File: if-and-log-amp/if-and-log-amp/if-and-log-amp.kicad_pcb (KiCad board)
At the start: 2 copper layers, 91.7 x 48.8 mm, 74 parts, among them J301 Coax, J305 Conn_01x03, J306 Conn_01x02, J307 Conn_Coaxial, Q301 2N3904, T301 FT37-43 8:2 t, U301 AD603AQ, U302 L78L05_TO92, U303 LM317L_TO92, U304 AD8307AN, U305 CA3140

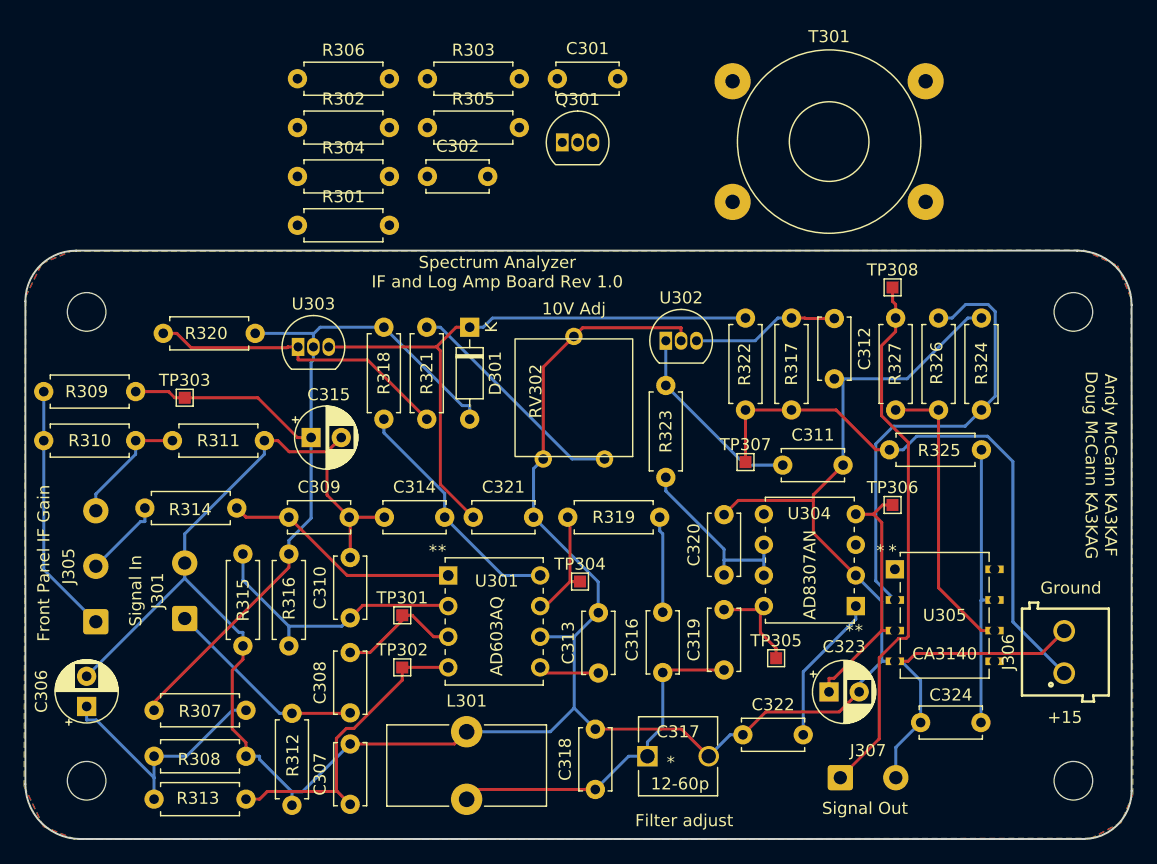
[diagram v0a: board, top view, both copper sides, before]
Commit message: improved if and log amp and second lo/mixer
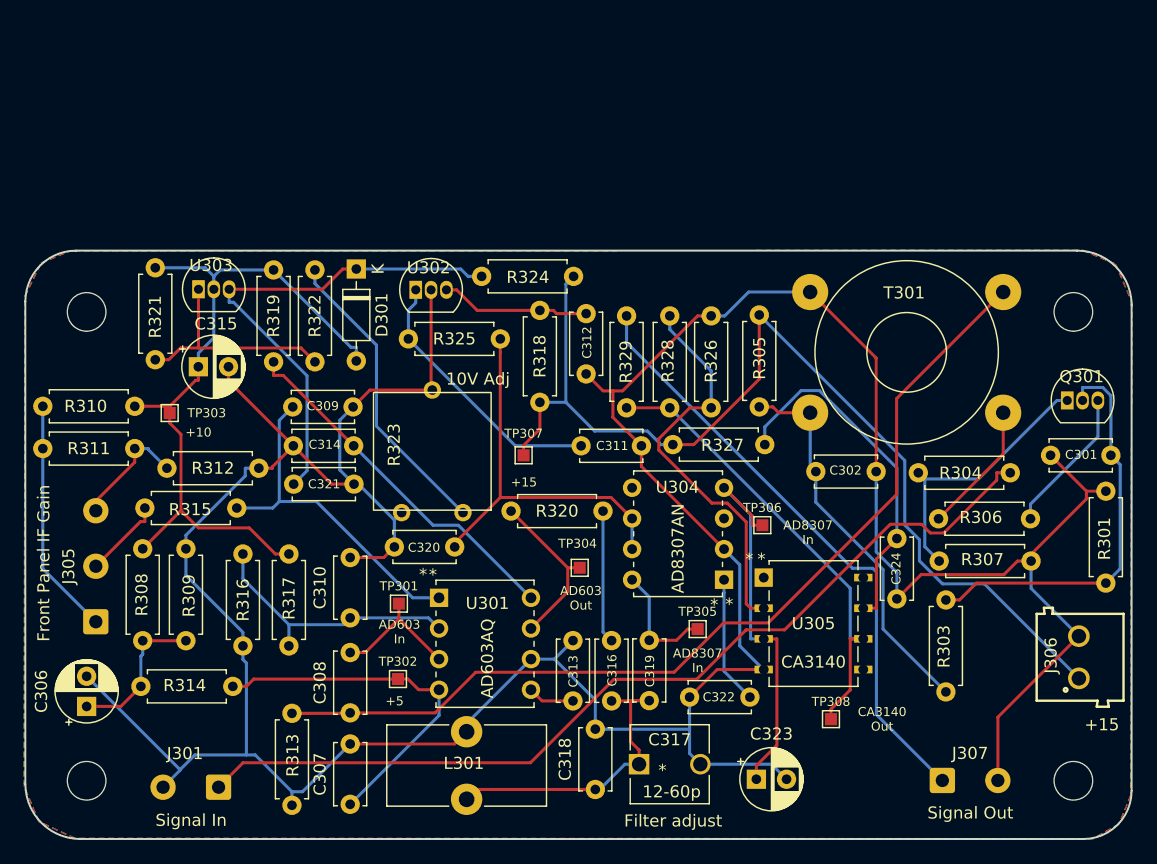
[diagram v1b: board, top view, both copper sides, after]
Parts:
- moved R301 76.9 mm to (184.9, 108.0), turned to 90 degrees
- moved R307 66.5 mm to (171.1, 106.1)
- moved R303 66.2 mm to (171.7, 117.0), turned to 90 degrees
- moved R306 53.4 mm to (171.0, 102.6)
- moved R304 52.2 mm to (169.4, 98.8)
- moved C301 51.4 mm to (180.3, 97.4)
- moved Q301 47.0 mm to (181.7, 92.8)
- moved C302 40.4 mm to (160.9, 98.7)
- moved R305 40.0 mm to (156.2, 85.8), turned to -90 degrees
- moved TP308 36.2 mm to (162.1, 119.3)
- moved C320 22.4 mm to (130.9, 105.0), turned to 180 degrees
- moved R326 22.4 mm to (152.2, 93.4)
- moved R329 22.3 mm to (145.2, 93.4)
- moved R328 22.3 mm to (148.8, 93.4)
- moved R325 21.7 mm to (127.1, 87.7), turned to 0 degrees
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- renumbered R302 to R301, R301 to R303, R303 to R304, R304 to R305, R305 to R306, R306 to R307, R307 to R308, R308 to R309, R309 to R310, R310 to R311, R311 to R312, R312 to R313, R313 to R314, R314 to R315, R315 to R316, R316 to R317, R317 to R318, R318 to R319, R319 to R320, R320 to R321, R321 to R322, RV302 to R323, R322 to R324, R323 to R325, R324 to R326, R325 to R327, R326 to R328, R327 to R329
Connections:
- R328 pad 1: Net-(R326-Pad1) (its old number) -> Net-(R328-Pad1)
- R329 pad 1: Net-(R326-Pad1) (its old number) -> Net-(R328-Pad1)
- TP308 pad 1: Net-(C325-Pad1) -> Net-(R328-Pad1)
- U305 pad 6: Net-(R326-Pad1) (its old number) -> Net-(R328-Pad1)
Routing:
- net /In: track 0.00 -> 77.4 mm
- net Net-(C308-Pad1): track 17.0 -> 78.1 mm
- net GND: track 251.6 -> 300.1 mm
- net Net-(R328-Pad1): track 0.00 -> 38.4 mm
- net /+15: track 48.5 -> 86.1 mm
- net Net-(C301-Pad2): track 0.00 -> 33.9 mm
- net Net-(C302-Pad1): track 0.00 -> 32.2 mm
- net Net-(R326-Pad1) (its old number): track 24.4 -> 0.00 mm
- net Net-(Q301-Pad1): track 0.00 -> 22.5 mm
- net Net-(C320-Pad1): track 15.9 -> 33.0 mm
- net /+10: track 74.6 -> 60.2 mm
- net Net-(Q301-Pad3): track 0.00 -> 12.1 mm
- net Net-(C323-Pad1): track 21.5 -> 32.8 mm
- net Net-(R306-Pad1): track 0.00 -> 11.0 mm
- net Net-(C314-Pad2): track 20.1 -> 30.1 mm
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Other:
- board text added: "+10"
- board text added: "+5"
- board text added: "AD603 In"
- board text added: "AD603 Out"
- board text added: "AD8307 In"
- board text added: "CA3140 Out"
- board text removed: "Ground"

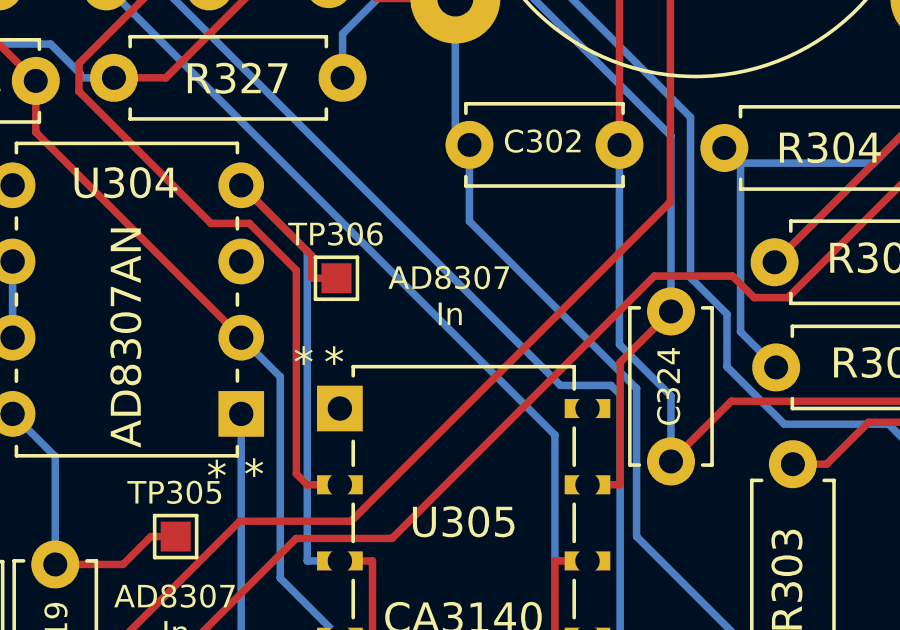
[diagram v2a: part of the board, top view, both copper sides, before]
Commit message: if and log amp - add version 0 pcb to directory
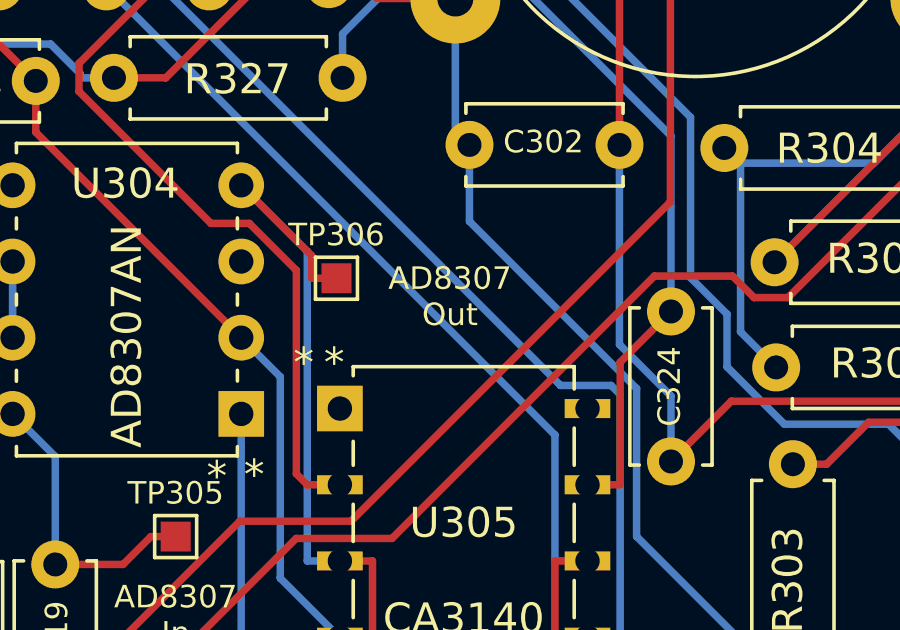
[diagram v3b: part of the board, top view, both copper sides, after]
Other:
- board text added: "AD8307 Out"
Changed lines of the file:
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@@
     (effects (font (size 0.75 0.75) (thickness 0.15)))
   )
-  (gr_text "AD8307\nIn" (at 160.2232 103.7844) (layer "F.SilkS")
+  (gr_text "AD8307\nOut" (at 160.2232 103.7844) (layer "F.SilkS")
     (effects (font (size 0.75 0.75) (thickness 0.15)))
   )

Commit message: IF Log Amp V2
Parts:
- removed C315: 22u, Capacitor_THT:CP_Radial_D5.0mm_P2.50mm
- removed C323: .001u, Capacitor_THT:CP_Radial_D5.0mm_P2.50mm
- removed C324: .1u, Capacitor_THT:C_Disc_D5.0mm_W2.5mm_P5.00mm
- removed J305: Conn_01x03, Connector_Wire:SolderWire-0.5sqmm_1x03_P4.6mm_D0.9mm_OD2.1mm
- removed J306: Conn_01x02, if-log-amp:691103110002
- removed J307: Conn_Coaxial, Connector_Wire:SolderWire-0.5sqmm_1x02_P4.6mm_D0.9mm_OD2.1mm
- removed R329: 1k, Resistor_THT:R_Axial_DIN0207_L6.3mm_D2.5mm_P7.62mm_Horizontal
- added C303: .1u, Capacitor_THT:C_Disc_D5.0mm_W2.5mm_P5.00mm, F.Cu at (101.1, 90.4)
- added C304: .01u, Capacitor_THT:C_Disc_D5.0mm_W2.5mm_P5.00mm, F.Cu at (123.8, 100.4)
- added C305: 100u, Capacitor_THT:CP_Radial_D5.0mm_P2.50mm, F.Cu at (148.4, 119.8)
- added J302: Conn_Coaxial, Connector_Wire:SolderWire-0.5sqmm_1x02_P4.6mm_D0.9mm_OD2.1mm, F.Cu at (166.6, 126.0)
- added J303: +15 In, spectrum analyzer:691103110002, F.Cu at (182.8, 95.3)
- added J304: Conn_01x03, Connector_Wire:SolderWire-0.5sqmm_1x03_P4.6mm_D0.9mm_OD2.1mm, F.Cu at (97.5, 110.3)
- added R302: 470, Resistor_THT:R_Axial_DIN0207_L6.3mm_D2.5mm_P7.62mm_Horizontal, F.Cu at (104.7, 110.4)
- added TP309: 803 +5, TestPoint:TestPoint_Pad_1.0x1.0mm, F.Cu at (167.5, 115.5)
- C306: value 100u -> .1u; footprint Capacitor_THT:CP_Radial_D5.0mm_P2.50mm -> Capacitor_THT:C_Disc_D5.0mm_W2.5mm_P5.00mm
- C308: value .01u -> .1u
- C309: value .1u -> 18p
- C311: value .1u -> 22u; footprint Capacitor_THT:C_Disc_D5.0mm_W2.5mm_P5.00mm -> Capacitor_THT:CP_Radial_D5.0mm_P2.50mm
- C312: value .22u -> 5.6p
- C313: value 18p -> 5-65pf; footprint Capacitor_THT:C_Disc_D5.0mm_W2.5mm_P5.00mm -> spectrum analyzer:BFC280831659
- C314: value .1u -> 220p
- C316: value 5.6p -> .1u
- C317: value 12-60p -> .1u; footprint if-log-amp:GKG60015 -> Capacitor_THT:C_Disc_D5.0mm_W2.5mm_P5.00mm
- C318: value 180p -> .1u
- C319: value 5.6p -> .22u
- C320: value .1u -> .001u
- C322: value .1u -> 5.6p
- D301: value 1N4150 -> 1N4148
- R301: value 2k -> 47
- R303: value 10k -> 2k
- R304: value 47 -> 10k
- R307: value 470 -> 100
- R310: value 680 -> 51
- R311: value 510 -> 680
- R312: value 1k -> 510
- R313: value 100 -> 1k
- R314: value 51 -> 2.2k
- R315: value 2.2k -> 5.6k
- R316: value 5.6k -> 4.3k
- R317: value 4.3k -> 1k
- R319: value 10 -> 220
- R320: value 1k -> 1.5k
- R321: value 220 -> 82
- R322: value 1.5k -> 10
- R323: value 100 -> 10; footprint if-log-amp:Potentiometer_Bourns_3386G_Vertical -> Resistor_THT:R_Axial_DIN0207_L6.3mm_D2.5mm_P7.62mm_Horizontal
- R324: value 10 -> 51
- R325: value 10 -> 680
- R326: value 680 -> 2.2k
- R327: value 51 -> 1k
- R328: value 2.2k -> 10
- T301: footprint Transformer_THT:Transformer_Toroid_Horizontal_D14.0mm_Amidon-T50 -> spectrum analyzer:Transformer Vertical 1P 1S
- TP301: value TestPoint -> 603 In
- TP302: value TestPoint -> 603 Pin 4
- TP303: value TestPoint -> 603 Pin 8
- TP304: value TestPoint -> 603 Out
- TP305: value TestPoint -> 803 In
- TP306: value TestPoint -> 803 Out
- TP307: value TestPoint -> +15
- TP308: value TestPoint -> CA3140 Out
- U301: footprint if-log-amp:AD603AQ -> spectrum analyzer:AD603AQ
- U302: value L78L05_TO92 -> AD8307; footprint Package_TO_SOT_THT:TO-92_Inline -> spectrum analyzer:AD8307AN
- U303: value LM317L_TO92 -> CA3140; footprint Package_TO_SOT_THT:TO-92_Inline -> spectrum analyzer:CA3140EZ
- U304: value AD8307AN -> LM317L_TO92; footprint if-log-amp:AD8307AN -> Package_TO_SOT_THT:TO-92_Inline
- U305: value CA3140 -> L78L05_TO92; footprint if-log-amp:CA3140EZ -> Package_TO_SOT_THT:TO-92_Inline
- moved H303 91.2 mm to (99.9, 124.9)
- moved R301 83.5 mm to (101.4, 110.4)
- moved Q301 82.7 mm to (101.6, 113.3), turned to -90 degrees
- moved H302 82.0 mm to (182.5, 84.7)
- moved C301 74.5 mm to (105.9, 99.3), turned to 180 degrees
- moved U303 70.1 mm to (173.1, 113.5), turned to 90 degrees
- moved R303 65.9 mm to (105.8, 119.8), turned to -90 degrees
- moved R304 60.2 mm to (110.3, 110.9), turned to -90 degrees
- moved R305 59.8 mm to (97.5, 97.3), turned to 90 degrees
- moved R306 58.0 mm to (113.6, 110.9), turned to -90 degrees
- moved C302 56.0 mm to (109.8, 121.6), turned to -90 degrees
- moved R325 54.4 mm to (173.2, 116.6), turned to -90 degrees
- moved C321 52.9 mm to (170.5, 100.2)
- moved R307 50.9 mm to (120.2, 104.0), turned to 90 degrees
- moved R310 48.6 mm to (143.4, 122.3), turned to 90 degrees
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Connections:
- C301 pad 1: GND -> Net-(J301-In)
- C302 pad 1: Net-(C302-Pad1) -> Net-(Q301-B)
- C306 pad 1: Net-(C306-Pad1) -> Net-(U301-COMM)
- C307 pad 1: Net-(C307-Pad1) -> Net-(U301-GPOS)
- C308 pad 1: Net-(C308-Pad1) -> Net-(U301-GNEG)
- C308 pad 2: Net-(C308-Pad2) -> GND
- C309 pad 1: Net-(C309-Pad1) -> Net-(U301-FDBK)
- C310 pad 1: Net-(C310-Pad1) -> GND
- C310 pad 2: GND -> Net-(U301-VPOS)
- C311 pad 1: /+5 -> /+10
- C312 pad 2: GND -> Net-(C312-Pad2)
- C313 pad 1: Net-(C313-Pad1) -> GND
- C313 pad 2: GND -> Net-(C312-Pad2)
- C314 pad 1: GND -> Net-(C312-Pad2)
- C314 pad 2: Net-(C314-Pad2) -> GND
- C316 pad 1: Net-(C316-Pad1) -> GND
- C316 pad 2: Net-(C316-Pad2) -> Net-(U302-INM)
- C317 pad 1: Net-(C316-Pad2) -> Net-(U302-ENB)
- C318 pad 1: Net-(C316-Pad2) -> /+5
- C319 pad 1: Net-(C316-Pad2) -> Net-(U305-VI)
- C319 pad 2: Net-(C319-Pad2) -> GND
- C320 pad 1: Net-(C320-Pad1) -> Net-(U302-OUT)
- C321 pad 1: Net-(C321-Pad1) -> GND
- C321 pad 2: GND -> Net-(U303-V+)
- C322 pad 1: GND -> Net-(C312-Pad2)
- C322 pad 2: Net-(C322-Pad2) -> Net-(U302-INP)
- D301 pad 1: Net-(C321-Pad1) -> Net-(D301-K)
- J301 pad 1: /In -> Net-(J301-In)
- L301 pad 2: Net-(C316-Pad2) -> Net-(C312-Pad2)
- Q301 pad 1: Net-(Q301-Pad1) -> Net-(Q301-E)
- Q301 pad 2: Net-(C301-Pad2) -> Net-(Q301-B)
- R301 pad 1: Net-(C301-Pad2) -> Net-(Q301-E)
- R301 pad 2: GND -> Net-(C301-Pad2)
- R303 pad 1: Net-(C302-Pad1) -> Net-(Q301-B)
- R303 pad 2: Net-(C301-Pad2) -> GND
- R304 pad 1: Net-(Q301-Pad1) -> Net-(T301-AA)
- R304 pad 2: /In -> Net-(Q301-B)
- R305 pad 2: Net-(C302-Pad1) -> Net-(T301-AA)
- R306 pad 1: Net-(R306-Pad1) -> Net-(T301-AB)
- R307 pad 1: Net-(Q301-Pad1) -> Net-(T301-SB)
- R308 pad 2: Net-(C306-Pad1) -> Net-(C305-Pad1)
- R309 pad 1: Net-(C306-Pad1) -> Net-(C305-Pad1)
- R310 pad 1: /+10 -> Net-(C305-Pad1)
- R310 pad 2: Net-(C303-Pad3) -> Net-(U301-COMM)
- R311 pad 1: Net-(C303-Pad3) -> /+10
- R312 pad 2: GND -> Net-(J304-Pin_3)
- R313 pad 1: Net-(C308-Pad1) -> Net-(J304-Pin_3)
- R314 pad 1: Net-(C306-Pad1) -> Net-(U301-GPOS)
- R314 pad 2: Net-(C307-Pad1) -> Net-(J304-Pin_2)
- R315 pad 1: Net-(C309-Pad1) -> Net-(U301-GNEG)
- R315 pad 2: Net-(C304-Pad3) -> GND
- R316 pad 1: Net-(C310-Pad1) -> Net-(U301-GNEG)
- R316 pad 2: GND -> /+10
- R317 pad 1: Net-(C310-Pad1) -> Net-(U301-VOUT)
- R317 pad 2: /+10 -> Net-(C312-Pad1)
- R318 pad 1: /+15 -> /+10
- R318 pad 2: Net-(C312-Pad1) -> Net-(U301-VPOS)
- R319 pad 2: Net-(C314-Pad2) -> Net-(U304-ADJ)
- R320 pad 1: Net-(R320-Pad1) -> Net-(U304-ADJ)
- R320 pad 2: Net-(C316-Pad1) -> Net-(R320-Pad2)
- R321 pad 1: /+10 -> Net-(R320-Pad2)
- R321 pad 2: Net-(R321-Pad2) -> GND
- R322 pad 1: Net-(R321-Pad2) -> /+5
- R322 pad 2: Net-(R322-Pad2) -> Net-(U302-ENB)
- R323 pad 1: Net-(R322-Pad2) -> /+15
- R323 pad 2: GND -> Net-(U305-VI)
- R324 pad 1: /+15 -> Net-(U303-V+)
- R324 pad 2: Net-(C321-Pad1) -> /+15
- R325 pad 1: /+5 -> Net-(U303--)
- R325 pad 2: Net-(C320-Pad1) -> GND
- R326 pad 2: GND -> Net-(U303--)
- R327 pad 1: Net-(C324-Pad2) -> Net-(R326-Pad1)
- R327 pad 2: /+15 -> Net-(J302-In)
- R328 pad 1: Net-(R328-Pad1) -> Net-(D301-K)
- R328 pad 2: Net-(R326-Pad1) -> /+15
- T301 pad 1: Net-(C302-Pad1) -> Net-(T301-AA)
- T301 pad 2: Net-(R306-Pad1) -> Net-(T301-SB)
- T301 pad 3: GND -> Net-(T301-AB)
- T301 pad 4: Net-(C308-Pad1) -> GND
- TP301 pad 1: Net-(C308-Pad2) -> Net-(U301-VINP)
- TP302 pad 1: Net-(C307-Pad1) -> Net-(U301-COMM)
- TP304 pad 1: Net-(R320-Pad1) -> Net-(U301-VOUT)
- TP305 pad 1: Net-(C319-Pad2) -> Net-(U302-INP)
- TP306 pad 1: Net-(C323-Pad1) -> Net-(U302-OUT)
- TP308 pad 1: Net-(R328-Pad1) -> Net-(R326-Pad1)
- U301 pad 1: Net-(C309-Pad1) -> Net-(U301-GPOS)
- U301 pad 2: Net-(C310-Pad1) -> Net-(U301-GNEG)
- U301 pad 3: Net-(C308-Pad2) -> Net-(U301-VINP)
- U301 pad 4: Net-(C307-Pad1) -> Net-(U301-COMM)
- U301 pad 5: Net-(C313-Pad1) -> Net-(U301-FDBK)
- U301 pad 7: Net-(R320-Pad1) -> Net-(U301-VOUT)
- U301 pad 8: Net-(C314-Pad2) -> Net-(U301-VPOS)
- U302 pad 1: /+5 -> Net-(U302-INM)
- U302 pad 3: Net-(C312-Pad1) -> unconnected-(U302-OFS-Pad3)
- U303 pad 1: Net-(R321-Pad2) -> unconnected-(U303-NULL-Pad1)
- U303 pad 2: /+10 -> Net-(U303--)
- U303 pad 3: Net-(C321-Pad1) -> Net-(U302-OUT)
- U304 pad 1: Net-(C322-Pad2) -> Net-(U304-ADJ)
- U304 pad 2: GND -> /+10
- U304 pad 3: unconnected-(U304-Pad3) -> Net-(D301-K)
- U305 pad 1: unconnected-(U305-Pad1) -> /+5
- U305 pad 2: Net-(R326-Pad1) -> GND
- U305 pad 3: Net-(C323-Pad1) -> Net-(U305-VI)
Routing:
- net Net-(C308-Pad1): track 78.1 -> 0.00 mm
- net /In: track 77.4 -> 0.00 mm
- net Net-(J304-Pin_3): track 0.00 -> 54.5 mm
- net Net-(C325-Pad1): track 50.3 -> 0.00 mm
- net Net-(C321-Pad1): track 41.4 -> 0.00 mm
- net Net-(U301-VINP): track 0.00 -> 39.8 mm
- net Net-(R328-Pad1): track 38.4 -> 0.00 mm
- net Net-(J301-In): track 0.00 -> 38.2 mm
- net Net-(C312-Pad2): track 0.00 -> 37.0 mm
- net Net-(C320-Pad1): track 33.0 -> 0.00 mm
- net Net-(C323-Pad1): track 32.8 -> 0.00 mm
- net Net-(C302-Pad1): track 32.2 -> 0.00 mm
- net Net-(C307-Pad1): track 30.3 -> 0.00 mm
- net Net-(C301-Pad2): track 33.9 -> 3.73 mm
- net Net-(C314-Pad2): track 30.1 -> 0.00 mm
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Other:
- board text added: "IF Gain"
- board text added: "IF Log Amp Rev 1"
- board text added: "In"
- board text added: "Out"
- board text removed: "+10"
- board text removed: "+5"
- board text removed: "10V Adj"
- board text removed: "AD603 In"
- board text removed: "AD603 Out"
- board text removed: "AD8307 In"
- board text removed: "AD8307 Out"
- board text removed: "CA3140 Out"
- board text removed: "Filter adjust"
- board text removed: "Front Panel IF Gain"
- board text removed: "Signal In"
- board text removed: "Signal Out"
- board text removed: "Spectrum Analyzer IF and Log Amp Board Rev 1.0"
